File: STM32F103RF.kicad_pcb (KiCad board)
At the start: 4 copper layers, 64.8 x 24.1 mm, 56 parts, among them J1 USB_C_Receptacle_USB2.0, J2 Conn_01x04, J3 Conn_Coaxial, U1 SPX3819M5-L-3-3, U2 STM32F103C6Tx, U3 NRF24L01, Y1 16MHz, Y2 16MHz

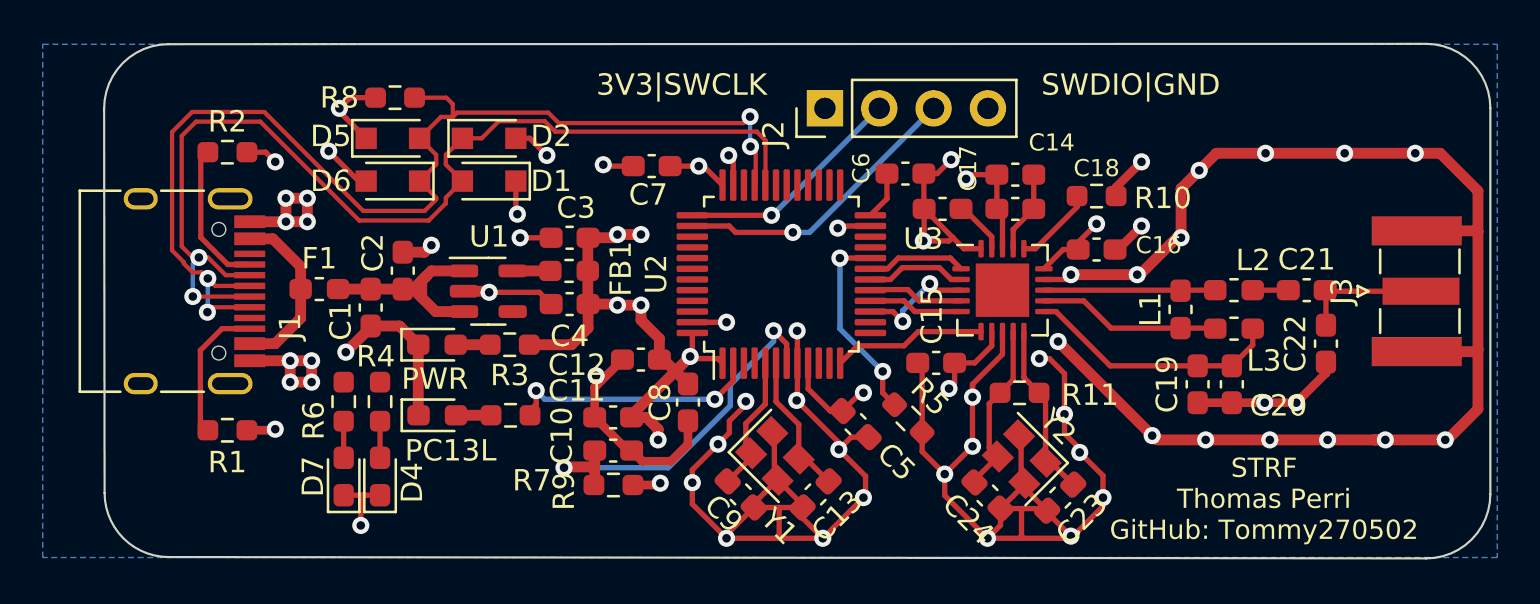
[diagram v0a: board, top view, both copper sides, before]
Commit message: fixed unconnected bottom side GND of connector and other missing connections
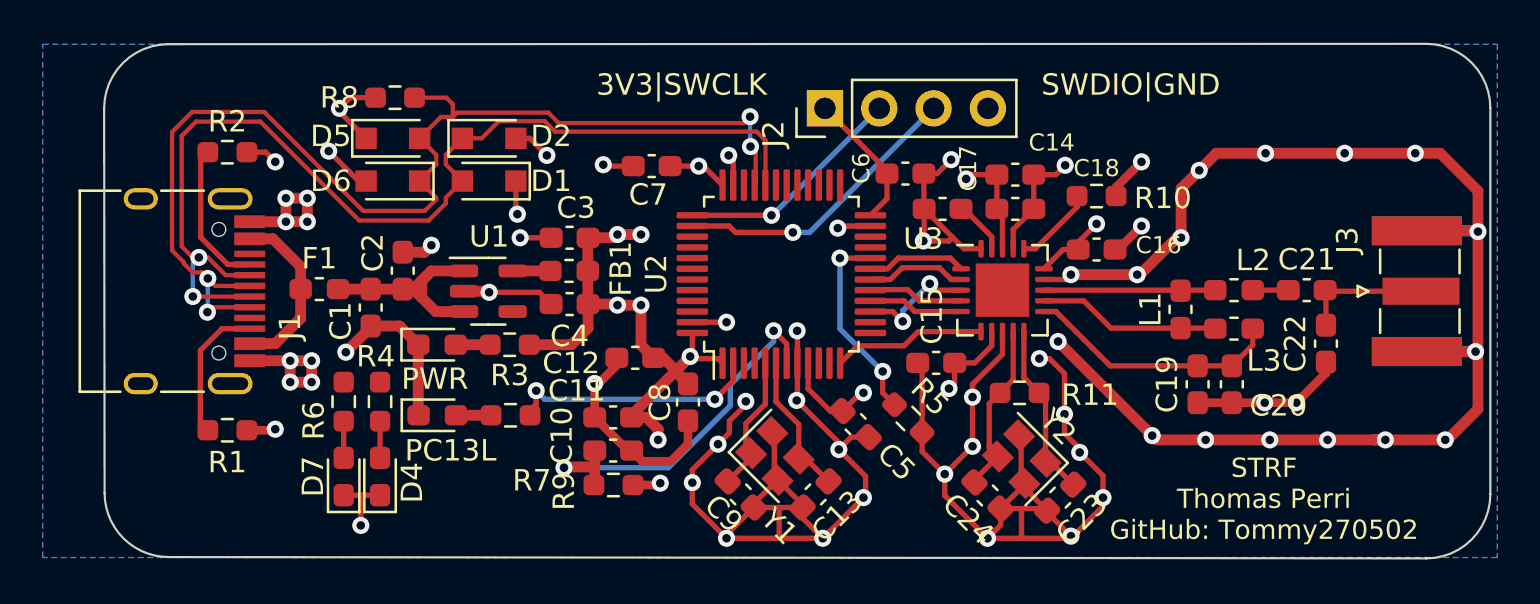
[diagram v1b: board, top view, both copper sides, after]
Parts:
- moved C12 0.28 mm to (92.1, 65.9)
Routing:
- net GND: track 225.3 -> 232.2 mm, vias 60 -> 63
- net 3.3V: track 54.8 -> 59.2 mm

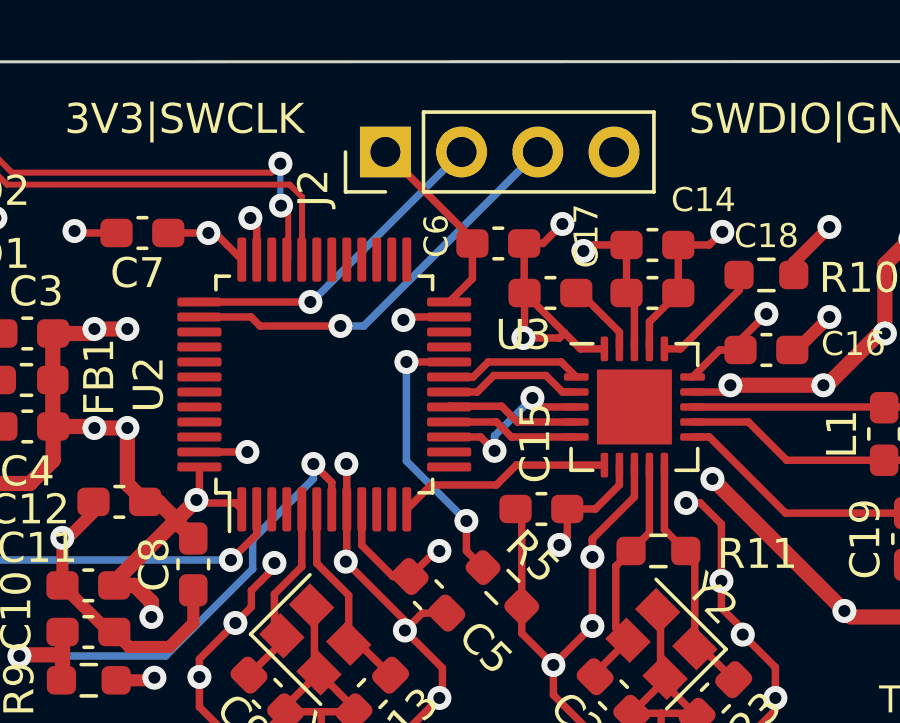
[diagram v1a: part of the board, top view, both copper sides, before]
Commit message: still fixing some polygons and shifting vias
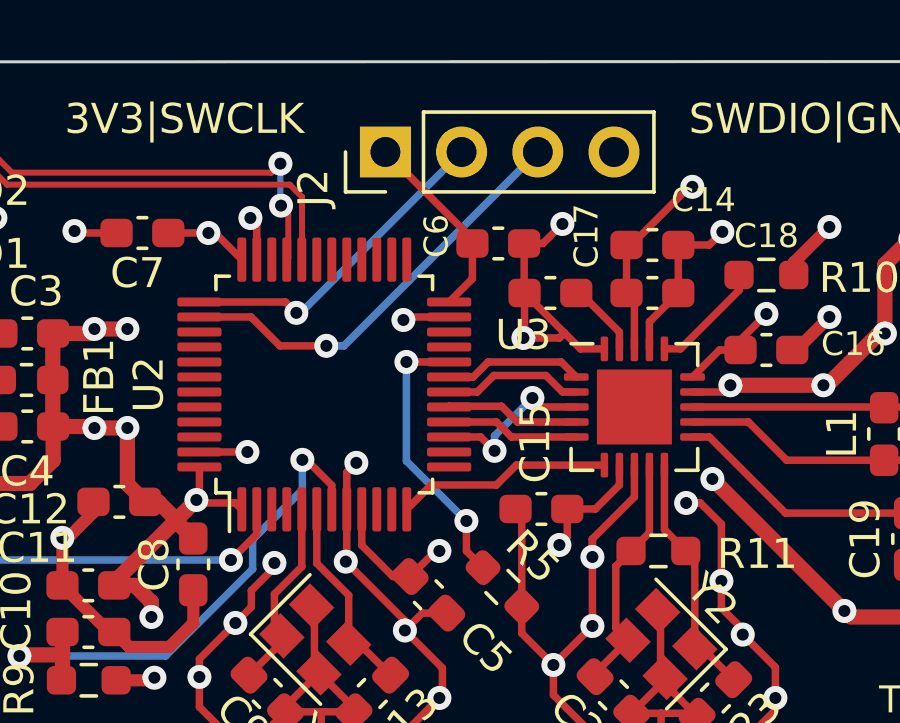
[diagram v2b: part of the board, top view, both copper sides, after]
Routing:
- net 3.3V: track 59.2 -> 60.7 mm
- net SWDIO: track 13.8 -> 14.4 mm
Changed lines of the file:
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@@
   (segment (start 114.58125 57.925) (end 115.76875 56.7375) (width 0.4064) (layer "F.Cu") (net 1))
   (segment (start 131.5 65.5) (end 131.3875 65.6125) (width 0.508) (layer "F.Cu") (net 1))
+  (segment (start 100 64.6) (end 99.68125 64.91875) (width 0.25) (layer "F.Cu") (net 1))
   (segment (start 85.21875 62.7875) (end 85.26875 62.8375) (width 0.508) (layer "F.Cu") (net 1))
   (segment (start 79.73125 64.475) (end 78.56875 65.6375) (width 0.508) (layer "F.Cu") (net 1))
@@
   (segment (start 101.61875 70.1875) (end 102.86875 71.4375) (width 0.25) (layer "F.Cu") (net 1))
   (segment (start 106.9375 60.26875) (end 105.60625 58.9375) (width 0.25) (layer "F.Cu") (net 1))
-  (segment (start 99.68125 66.15) (end 99.68125 64.65) (width 0.25) (layer "F.Cu") (net 1))
   (segment (start 112.881 70.32525) (end 112.881 70.14975) (width 0.25) (layer "F.Cu") (net 1))
   (segment (start 90.203125 67.284375) (end 91.503125 65.984375) (width 0.4064) (layer "F.Cu") (net 1))
-  (segment (start 99.68125 64.65) (end 99.66875 64.6375) (width 0.25) (layer "F.Cu") (net 1))
   (segment (start 131.5 58.1) (end 131.5 60) (width 0.508) (layer "F.Cu") (net 1))
   (segment (start 127.16875 69.7375) (end 126.6625 69.7375) (width 0.508) (layer "F.Cu") (net 1))
@@
   (segment (start 100.86875 74.3375) (end 98.86875 74.3375) (width 0.25) (layer "F.Cu") (net 1))
   (segment (start 114.58125 58.3375) (end 114.58125 57.925) (width 0.4064) (layer "F.Cu") (net 1))
+  (segment (start 99.68125 64.91875) (end 99.68125 66.15) (width 0.25) (layer "F.Cu") (net 1))
   (segment (start 87.16875 55.6375) (end 86.51875 55.6375) (width 0.25) (layer "F.Cu") (net 1))
   (segment (start 110.139717 71.598416) (end 110.292494 71.751193) (width 0.25) (layer "F.Cu") (net 1))
@@
   (via (at 96.46875 56.4375) (size 0.8) (drill 0.4) (layers "F.Cu" "B.Cu") (net 1))
   (via (at 101.56875 59.8375) (size 0.8) (drill 0.4) (layers "F.Cu" "B.Cu") (net 1))
-  (via (at 99.66875 64.6375) (size 0.8) (drill 0.4) (layers "F.Cu" "B.Cu") (net 1))
+  (via (at 100 64.6) (size 0.8) (drill 0.4) (layers "F.Cu" "B.Cu") (net 1))
   (via (at 96.36875 74.3375) (size 0.8) (drill 0.4) (layers "F.Cu" "B.Cu") (net 1))
   (via (at 129.96875 69.7375) (size 0.8) (drill 0.4) (layers "F.Cu" "B.Cu") (net 1))
@@
   (segment (start 109.00625 57.3375) (end 109.00625 58.9375) (width 0.25) (layer "F.Cu") (net 2))
   (segment (start 93.73125 56.9375) (end 95.06875 56.9375) (width 0.25) (layer "F.Cu") (net 2))
-  (segment (start 109.00625 57.3375) (end 107.578097 57.3375) (width 0.25) (layer "F.Cu") (net 2))
   (segment (start 107.03125 67.075) (end 107.03125 66.1375) (width 0.25) (layer "F.Cu") (net 2))
   (segment (start 95.29375 56.9375) (end 96.18125 57.825) (width 0.25) (layer "F.Cu") (net 2))
@@
   (segment (start 103.86875 57.2875) (end 103.86875 57.1375) (width 0.25) (layer "F.Cu") (net 2))
   (segment (start 94.76875 65.9375) (end 94.66875 65.8375) (width 0.25) (layer "F.Cu") (net 2))
-  (segment (start 107.578097 57.3375) (end 107.519218 57.396379) (width 0.25) (layer "F.Cu") (net 2))
   (segment (start 94.76875 64.7375) (end 94.76875 65.7375) (width 0.25) (layer "F.Cu") (net 2))
   (segment (start 100.18125 67.35) (end 101.220135 68.388885) (width 0.25) (layer "F.Cu") (net 2))
@@
   (segment (start 93.975 66.475) (end 93.975 66.53125) (width 0.508) (layer "F.Cu") (net 2))
   (segment (start 103.86875 57.2875) (end 103.86875 58.4625) (width 0.25) (layer "F.Cu") (net 2))
+  (segment (start 109.1625 57.3375) (end 109.00625 57.3375) (width 0.25) (layer "F.Cu") (net 2))
+  (segment (start 111.2 55.4) (end 111.1 55.4) (width 0.25) (layer "F.Cu") (net 2))
   (segment (start 107.96875 66.1375) (end 107.03125 66.1375) (width 0.25) (layer "F.Cu") (net 2))
   (segment (start 93.975 66.53125) (end 94.565625 67.121875) (width 0.508) (layer "F.Cu") (net 2))
@@
   (segment (start 78.76875 53.7375) (end 78.26875 54.2375) (width 0.25) (layer "F.Cu") (net 2))
   (segment (start 109.00625 58.9375) (end 109.26875 59.2) (width 0.25) (layer "F.Cu") (net 2))
+  (segment (start 111.1 55.4) (end 109.1625 57.3375) (width 0.25) (layer "F.Cu") (net 2))
   (segment (start 89.88125 63.375) (end 89.89375 63.3875) (width 0.508) (layer "F.Cu") (net 2))
   (segment (start 92.615625 68.684375) (end 93.16875 69.2375) (width 0.508) (layer "F.Cu") (net 2))
@@
   (via (at 91.26875 60.1375) (size 0.8) (drill 0.4) (layers "F.Cu" "B.Cu") (net 2))
   (via (at 91.26875 63.4375) (size 0.8) (drill 0.4) (layers "F.Cu" "B.Cu") (net 2))
-  (via (at 107.56875 57.5375) (size 0.8) (drill 0.4) (layers "F.Cu" "B.Cu") (net 2))
+  (via (at 111.2 55.4) (size 0.8) (drill 0.4) (layers "F.Cu" "B.Cu") (net 2))
+  (segment (start 98.2 64.5) (end 98.333756 64.5) (width 0.25) (layer "F.Cu") (net 4))
   (segment (start 90.20625 71.81) (end 90.16875 71.8475) (width 0.508) (layer "F.Cu") (net 4))
-  (segment (start 99.18125 66.15) (end 99.18125 65.25) (width 0.25) (layer "F.Cu") (net 4))
   (segment (start 90.20625 71) (end 90.20625 71.81) (width 0.508) (layer "F.Cu") (net 4))
   (segment (start 90.20625 71) (end 88.80625 71) (width 0.508) (layer "F.Cu") (net 4))
   (segment (start 90.20625 70.2375) (end 90.20625 71) (width 0.508) (layer "F.Cu") (net 4))
-  (segment (start 99.18125 65.25) (end 98.56875 64.6375) (width 0.25) (layer "F.Cu") (net 4))
+  (segment (start 99.18125 65.347494) (end 99.18125 66.15) (width 0.25) (layer "F.Cu") (net 4))
+  (segment (start 98.333756 64.5) (end 99.18125 65.347494) (width 0.25) (layer "F.Cu") (net 4))
   (segment (start 88.80625 71) (end 88.76875 71.0375) (width 0.508) (layer "F.Cu") (net 4))
   (via (at 88.76875 71.0375) (size 0.8) (drill 0.4) (layers "F.Cu" "B.Cu") (net 4))
-  (via (at 98.56875 64.6375) (size 0.8) (drill 0.4) (layers "F.Cu" "B.Cu") (net 4))
-  (segment (start 98.56875 65.13125) (end 96.54425 67.15575) (width 0.25) (layer "B.Cu") (net 4))
-  (segment (start 98.56875 64.6375) (end 98.56875 65.13125) (width 0.25) (layer "B.Cu") (net 4))
-  (segment (start 93.644353 71.0375) (end 88.76875 71.0375) (width 0.25) (layer "B.Cu") (net 4))
+  (via (at 98.2 64.5) (size 0.8) (drill 0.4) (layers "F.Cu" "B.Cu") (net 4))
+  (segment (start 98.2 65.5) (end 96.54425 67.15575) (width 0.25) (layer "B.Cu") (net 4))
+  (segment (start 98.2 64.5) (end 98.2 65.5) (width 0.25) (layer "B.Cu") (net 4))
   (segment (start 96.54425 68.137603) (end 93.644353 71.0375) (width 0.25) (layer "B.Cu") (net 4))
   (segment (start 96.54425 67.15575) (end 96.54425 68.137603) (width 0.25) (layer "B.Cu") (net 4))
+  (segment (start 93.644353 71.0375) (end 88.76875 71.0375) (width 0.25) (layer "B.Cu") (net 4))
   (segment (start 83.70625 65.2875) (end 85.31875 65.2875) (width 0.508) (layer "F.Cu") (net 5))
   (segment (start 87.46875 68.075) (end 86.95625 68.5875) (width 0.25) (layer "F.Cu") (net 6))
@@
   (segment (start 112.75625 58.85) (end 112.75625 58.3375) (width 0.25) (layer "F.Cu") (net 57))
   (segment (start 110.80625 60.8) (end 112.75625 58.85) (width 0.25) (layer "F.Cu") (net 57))
-  (segment (start 98.46875 59.237511) (end 98.468739 59.2375) (width 0.25) (layer "F.Cu") (net 58))
-  (segment (start 98.468739 59.2375) (end 94.76875 59.2375) (width 0.25) (layer "F.Cu") (net 58))
-  (via (at 98.46875 59.237511) (size 0.8) (drill 0.4) (layers "F.Cu" "B.Cu") (net 58))
-  (segment (start 98.46875 59.237511) (end 98.508739 59.237511) (width 0.25) (layer "B.Cu") (net 58))
-  (segment (start 98.508739 59.237511) (end 103.50875 54.2375) (width 0.25) (layer "B.Cu") (net 58))
-  (segment (start 96.790813 60.0375) (end 96.490813 59.7375) (width 0.25) (layer "F.Cu") (net 59))
-  (segment (start 99.46875 60.0375) (end 96.790813 60.0375) (width 0.25) (layer "F.Cu") (net 59))
+  (segment (start 98 59.6) (end 97.6375 59.2375) (width 0.25) (layer "F.Cu") (net 58))
+  (segment (start 97.6375 59.2375) (end 94.76875 59.2375) (width 0.25) (layer "F.Cu") (net 58))
+  (via (at 98 59.6) (size 0.8) (drill 0.4) (layers "F.Cu" "B.Cu") (net 58))
+  (segment (start 98 59.6) (end 98.14625 59.6) (width 0.25) (layer "B.Cu") (net 58))
+  (segment (start 98.14625 59.6) (end 103.50875 54.2375) (width 0.25) (layer "B.Cu") (net 58))
+  (segment (start 97.453313 60.7) (end 96.490813 59.7375) (width 0.25) (layer "F.Cu") (net 59))
+  (segment (start 99 60.7) (end 97.453313 60.7) (width 0.25) (layer "F.Cu") (net 59))
   (segment (start 96.490813 59.7375) (end 94.76875 59.7375) (width 0.25) (layer "F.Cu") (net 59))
-  (via (at 99.46875 60.0375) (size 0.8) (drill 0.4) (layers "F.Cu" "B.Cu") (net 59))
-  (segment (start 99.46875 60.0375) (end 100.24875 60.0375) (width 0.25) (layer "B.Cu") (net 59))
-  (segment (start 100.24875 60.0375) (end 106.04875 54.2375) (width 0.25) (layer "B.Cu") (net 59))
+  (via (at 99 60.7) (size 0.8) (drill 0.4) (layers "F.Cu" "B.Cu") (net 59))
+  (segment (start 99 60.7) (end 99.58625 60.7) (width 0.25) (layer "B.Cu") (net 59))
+  (segment (start 99.58625 60.7) (end 106.04875 54.2375) (width 0.25) (layer "B.Cu") (net 59))
   (segment (start 76.45625 61.635478) (end 75.158272 60.3375) (width 0.508) (layer "F.Cu") (net 60))
   (segment (start 76.45625 62.6875) (end 76.45625 61.635478) (width 0.508) (layer "F.Cu") (net 60))
@@
     (connect_pads (clearance 0.508))
     (min_thickness 0.254) (filled_areas_thickness no)
-    (fill yes (thermal_gap 0.508) (thermal_bridge_width 0.508))
+    (fill yes (mode hatch) (thermal_gap 0.508) (thermal_bridge_width 0.508)
+      (hatch_thickness 0.254) (hatch_gap 0.254) (hatch_orientation 0)
+      (hatch_border_algorithm hatch_thickness) (hatch_min_hole_area 0.3))
     (polygon
       (pts

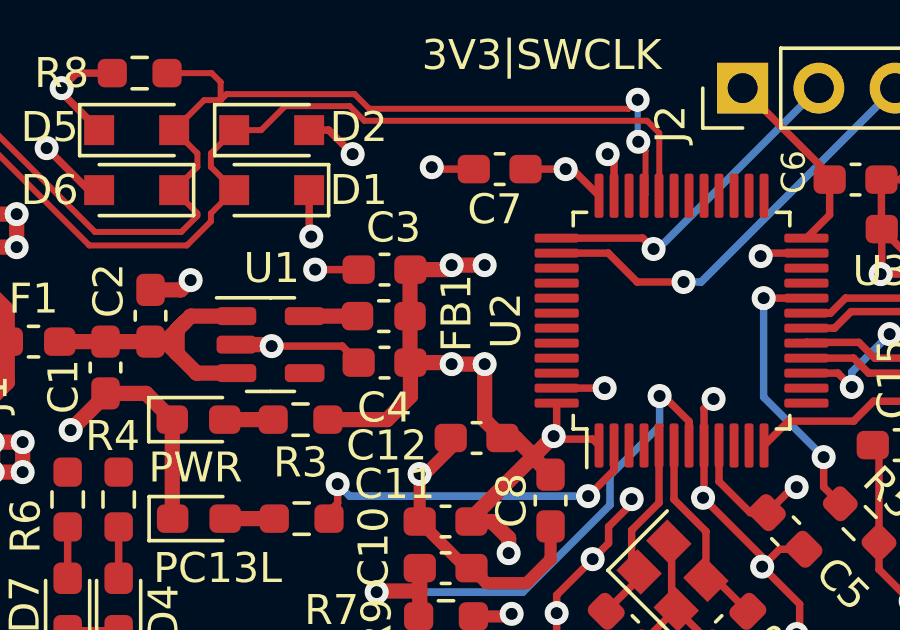
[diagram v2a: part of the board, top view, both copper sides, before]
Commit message: redid some power vias
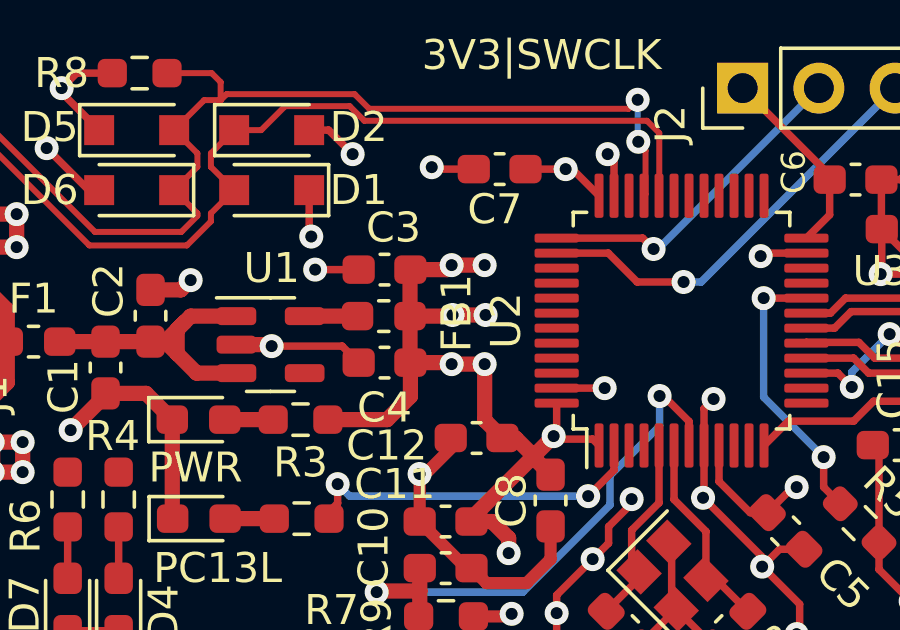
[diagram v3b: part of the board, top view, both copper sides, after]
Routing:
- net 3.3V: track 60.7 -> 63.2 mm, vias 14 -> 16
- added copper zone on In2.Cu, net 3.3V
- added copper zone on B.Cu, net GND
- removed copper zone on B.Cu, net 3.3V
- removed copper zone on In2.Cu, net GND
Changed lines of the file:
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@@
   (segment (start 89.89375 63.3875) (end 91.21875 63.3875) (width 0.508) (layer "F.Cu") (net 2))
   (segment (start 96.18125 66.15) (end 95.96875 65.9375) (width 0.25) (layer "F.Cu") (net 2))
+  (segment (start 91.2625 61.8375) (end 91.3 61.8) (width 0.508) (layer "F.Cu") (net 2))
   (segment (start 103.86875 57.1375) (end 100.96875 54.2375) (width 0.25) (layer "F.Cu") (net 2))
   (segment (start 91.99375 71.8475) (end 93.18325 71.8475) (width 0.4064) (layer "F.Cu") (net 2))
@@
   (segment (start 91.928125 68.684375) (end 92.615625 68.684375) (width 0.508) (layer "F.Cu") (net 2))
   (segment (start 89.88125 60.3) (end 89.89375 60.2875) (width 0.508) (layer "F.Cu") (net 2))
+  (segment (start 91.3 61.8) (end 92.4 61.8) (width 0.508) (layer "F.Cu") (net 2))
+  (segment (start 89.88125 61.8375) (end 91.2625 61.8375) (width 0.508) (layer "F.Cu") (net 2))
   (segment (start 78.26875 54.3875) (end 79.51875 55.6375) (width 0.25) (layer "F.Cu") (net 2))
   (segment (start 78.76875 53.7375) (end 78.26875 54.2375) (width 0.25) (layer "F.Cu") (net 2))
@@
   (via (at 92.36875 60.1375) (size 0.8) (drill 0.4) (layers "F.Cu" "B.Cu") (net 2))
   (via (at 92.36875 63.4375) (size 0.8) (drill 0.4) (layers "F.Cu" "B.Cu") (net 2))
+  (via (at 91.3 61.8) (size 0.8) (drill 0.4) (layers "F.Cu" "B.Cu") (net 2))
   (via (at 106.76875 67.3375) (size 0.8) (drill 0.4) (layers "F.Cu" "B.Cu") (net 2))
+  (via (at 92.4 61.8) (size 0.8) (drill 0.4) (layers "F.Cu" "B.Cu") (net 2))
   (via (at 102.76875 67.5375) (size 0.8) (drill 0.4) (layers "F.Cu" "B.Cu") (net 2))
   (via (at 86.589056 59.18477) (size 0.8) (drill 0.4) (layers "F.Cu" "B.Cu") (net 2))
@@
     )
   )
-  (zone (net 1) (net_name "GND") (layer "In2.Cu") (hatch edge 0.508)
+  (zone (net 2) (net_name "3.3V") (layer "In2.Cu") (hatch edge 0.508)
     (connect_pads (clearance 0.508))
     (min_thickness 0.254) (filled_areas_thickness no)
@@
     )
   )
-  (zone (net 2) (net_name "3.3V") (layer "B.Cu") (hatch edge 0.508)
+  (zone (net 1) (net_name "GND") (layer "B.Cu") (hatch edge 0.508)
     (connect_pads (clearance 0.508))
     (min_thickness 0.254) (filled_areas_thickness no)
